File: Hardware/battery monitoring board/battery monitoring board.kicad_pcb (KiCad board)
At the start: 2 copper layers, 190.5 x 53.3 mm, 69 parts, among them J1 Conn_01x02, J2 Conn_01x02, J3 S5B-XH-A, J4 Conn_01x02, J5 Conn_01x02, J6 Conn_01x02, J7 Conn_01x02, J8 Conn_01x02, J9 S5B-XH-A, K1 Relay_SPST-NO, Q1 PNP, Q2 PN2222A, U1 MAX31855KASA

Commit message: Added more parts
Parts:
- moved J5 90.3 mm to (87.6, 43.2), turned to -90 degrees
- moved J4 87.3 mm to (88.9, 30.5), turned to -90 degrees
- moved J6 79.9 mm to (87.6, 50.8), turned to -90 degrees
- moved J7 69.6 mm to (87.6, 58.4), turned to -90 degrees
- moved J8 59.4 mm to (87.6, 66.0), turned to -90 degrees
- moved TP14 53.0 mm to (123.4, 27.2), turned to 90 degrees
- moved R23 46.8 mm to (114.8, 35.6), turned to 90 degrees
- moved R19 46.7 mm to (114.8, 23.9), turned to -90 degrees
- moved R21 46.6 mm to (114.8, 30.5), turned to -90 degrees
- moved R17 45.9 mm to (112.8, 39.9)
- moved TP15 45.1 mm to (119.9, 27.2), turned to 90 degrees
- moved R22 42.8 mm to (111.3, 35.6), turned to 90 degrees
- moved R18 42.8 mm to (111.3, 23.9), turned to 90 degrees
- moved R20 42.7 mm to (111.3, 30.5), turned to -90 degrees
- moved TP16 34.7 mm to (118.4, 43.9)
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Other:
- board size 190.5 x 53.3 mm -> 134.6 x 53.3 mm

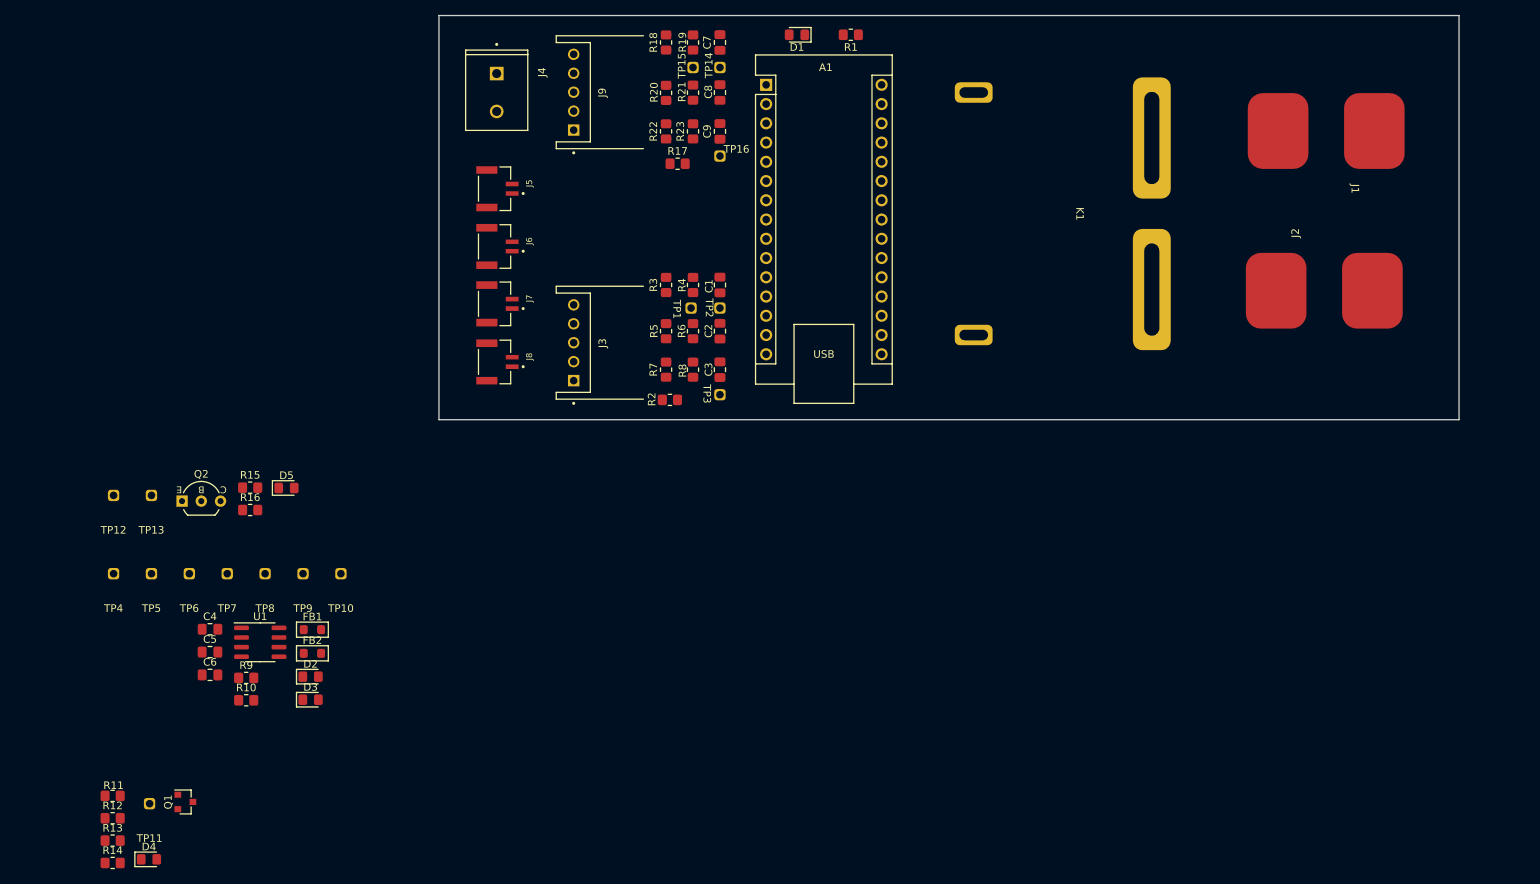
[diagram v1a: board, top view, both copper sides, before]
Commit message: place leak sensor and temp sensor on the pcb
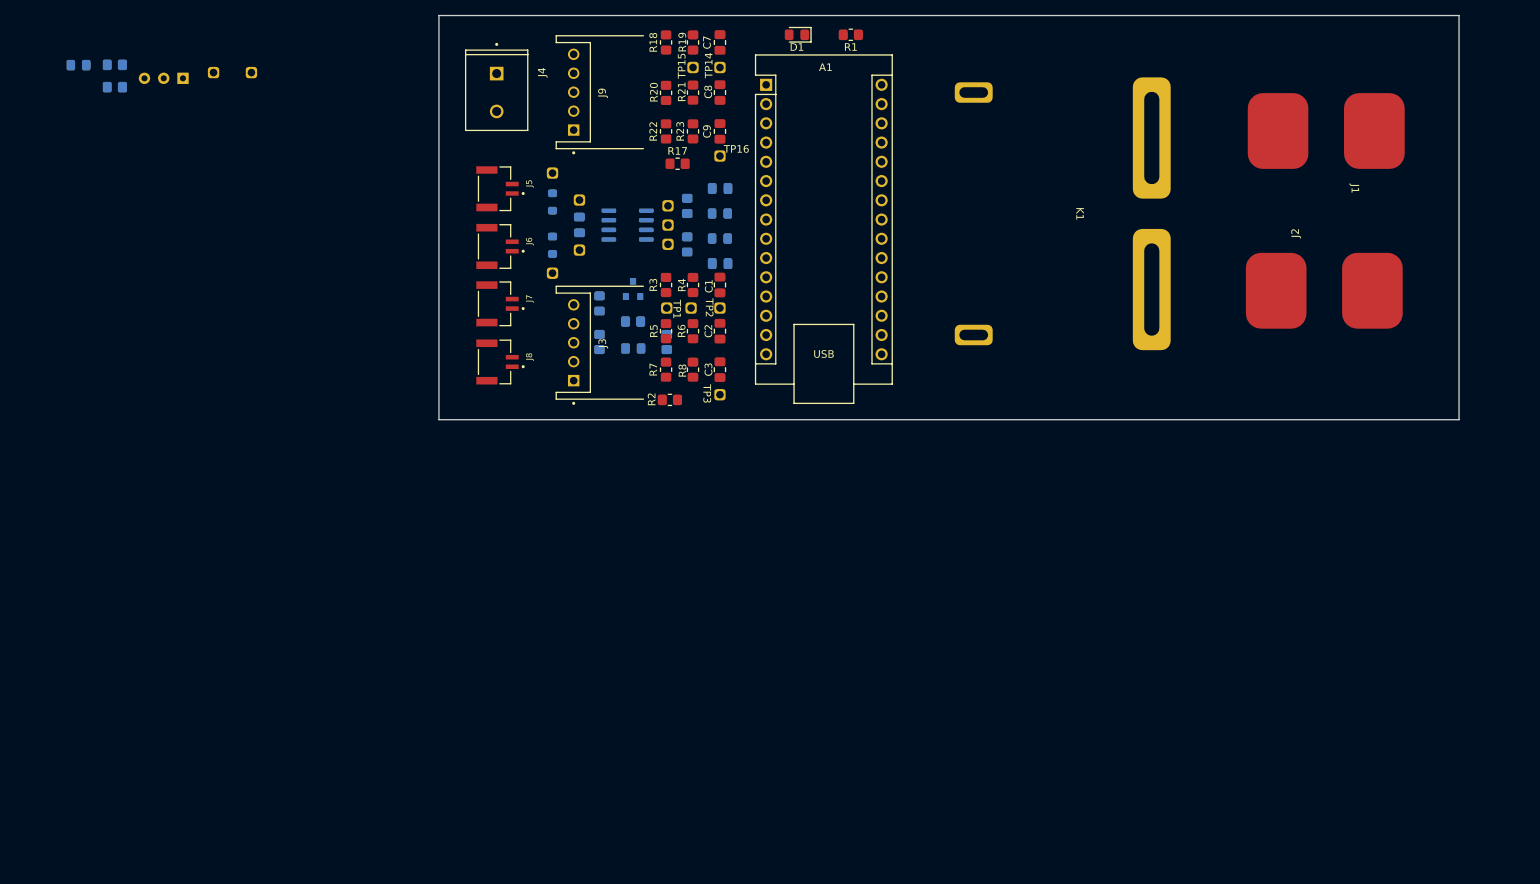
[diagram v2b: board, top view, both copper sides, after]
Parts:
- C4, C5, C6, D2, D3, D4, D5, FB1, FB2, Q1, Q2, R10, R11, R12, R13, R14, R15, R16, R9, TP10, TP11, TP12, TP13, TP4, TP5, TP6, TP7, TP8, TP9, U1: moved to B.Cu
- moved R14 100.4 mm to (111.3, 63.4), turned to -90 degrees
- moved R13 97.0 mm to (106.9, 60.7), turned to 180 degrees
- moved TP11 94.5 mm to (111.3, 64.0), turned to 180 degrees
- moved R12 93.5 mm to (102.5, 58.3), turned to -90 degrees
- moved D4 92.9 mm to (106.9, 64.3)
- moved C5 91.0 mm to (118.4, 43.1), turned to 180 degrees
- moved Q1 89.9 mm to (106.9, 56.4), turned to 90 degrees
- moved R11 87.8 mm to (102.5, 63.4), turned to 90 degrees
- moved C6 86.5 mm to (118.4, 53.1), turned to 180 degrees
- moved R9 85.2 mm to (114.0, 45.5), turned to -90 degrees
- moved R10 83.7 mm to (114.0, 50.5), turned to -90 degrees
- moved D2 81.6 mm to (118.4, 46.5), turned to 180 degrees
- moved D3 81.4 mm to (118.4, 49.8), turned to 180 degrees
- moved TP4 78.4 mm to (96.3, 46.2), turned to 180 degrees
- moved U1 73.4 mm to (106.2, 48.0)
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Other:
- copper layers 2 -> 4

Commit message: Added screw holes + other stuff
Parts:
- added ?: , , F.Cu at (83.8, 71.1)
- added ?: , , F.Cu at (213.6, 71.4)
- added ?: , , F.Cu at (213.4, 22.9)
- added J10: Conn_01x02, Library:JST_BM02B-GHS-TBT_LF__SN_, F.Cu at (88.4, 24.6)
- added REF**: Screw_Holes, Library:Screw_Holes, F.Cu at (83.8, 25.4)
- moved D5 128.3 mm to (160.5, 46.5), turned to -90 degrees
- moved TP13 116.6 mm to (159.5, 77.0)
- moved R16 112.6 mm to (149.4, 49.5), turned to -90 degrees
- moved R15 111.3 mm to (148.3, 45.0), turned to 0 degrees
- moved Q2 108.4 mm to (155.0, 42.3), turned to -90 degrees
- moved TP12 100.1 mm to (146.6, 76.7)
- moved J4 4.58 mm to (88.6, 35.1)
- moved J5 2.18 mm to (88.4, 45.2)
- moved J6 2.18 mm to (88.4, 52.8)
- moved J7 2.18 mm to (88.4, 60.4)
- moved J8 2.18 mm to (88.4, 68.1)
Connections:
- net +9V renamed Net-(D5-K)
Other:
- outline, holes or cut-outs redrawn

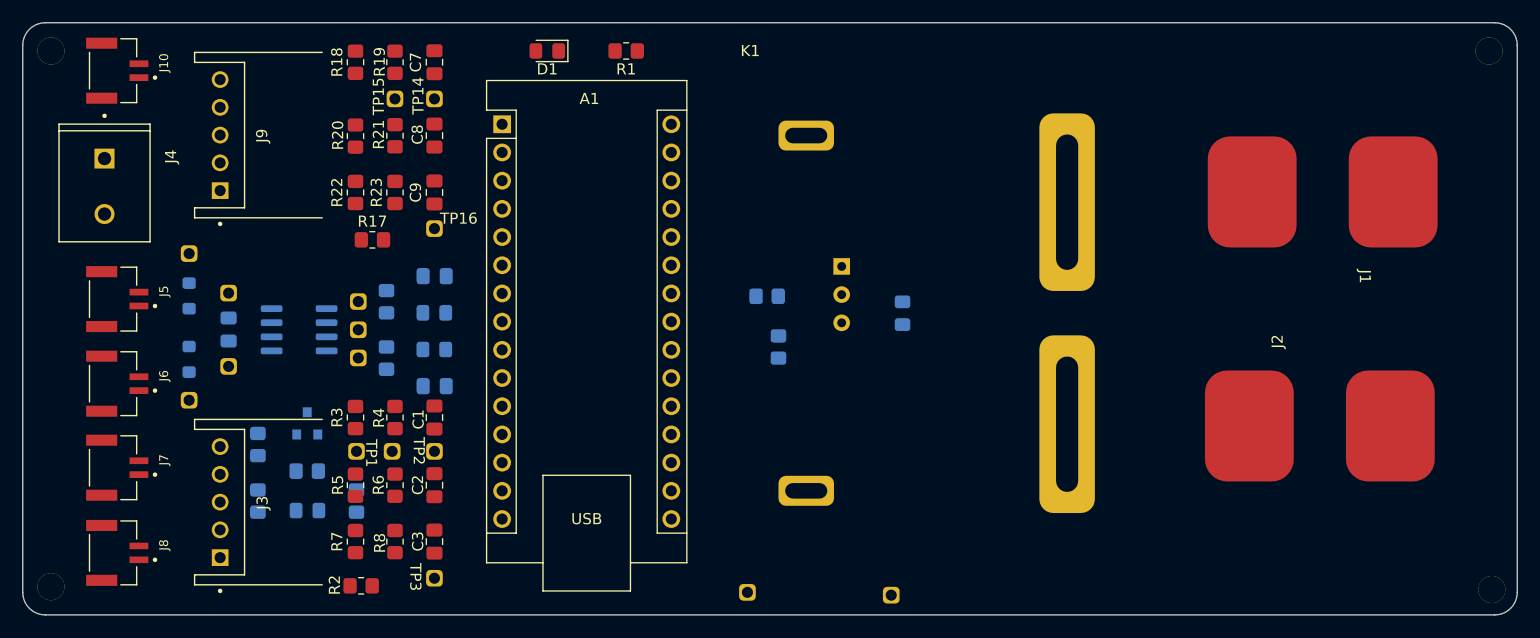
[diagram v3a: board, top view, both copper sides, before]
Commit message: Added traces pt.I
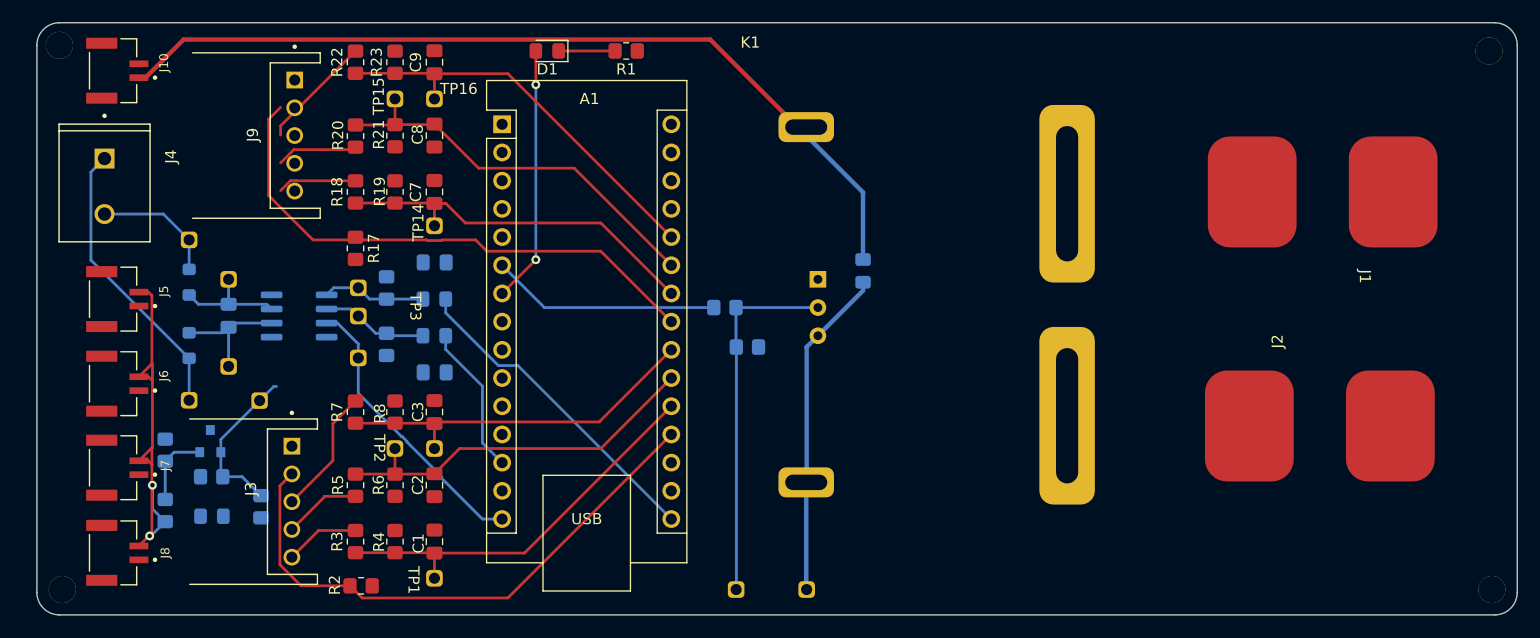
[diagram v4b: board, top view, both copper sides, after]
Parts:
- moved TP1 12.0 mm to (113.3, 70.4)
- moved C9 11.7 mm to (118.4, 23.9)
- moved R22 11.7 mm to (111.3, 23.9)
- moved R23 11.7 mm to (114.8, 23.9)
- moved TP3 11.7 mm to (113.3, 58.7)
- moved C7 11.7 mm to (118.4, 35.6)
- moved R18 11.7 mm to (111.3, 35.6)
- moved R19 11.7 mm to (114.8, 35.6)
- moved TP16 11.7 mm to (118.4, 32.3)
- moved C3 11.7 mm to (118.4, 55.4)
- moved R7 11.7 mm to (111.3, 55.4)
- moved R8 11.7 mm to (114.8, 55.4)
- moved TP14 11.4 mm to (123.4, 38.6)
- moved C1 11.2 mm to (118.4, 67.1)
- moved R3 11.2 mm to (111.3, 67.1)
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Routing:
- net Net-(D5-K): track 0.00 -> 78.4 mm
- net /voltage monitor/OUT1: track 0.00 -> 51.2 mm
- net /voltage monitor2/OUT1: track 0.00 -> 49.4 mm
- net /voltage monitor2/OUT4: track 0.00 -> 36.8 mm
- net /voltage monitor/OUT2: track 0.00 -> 36.2 mm
- net /leak sensor/PROBE: track 0.00 -> 36.1 mm, vias 0 -> 2
- net /voltage monitor2/OUT3: track 0.00 -> 36.1 mm
- net /voltage monitor/OUT3: track 0.00 -> 34.3 mm
- net /voltage monitor2/OUT2: track 0.00 -> 34.1 mm
- net /voltage monitor/OUT4: track 0.00 -> 33.5 mm
- net Net-(Q2-B): track 0.00 -> 33.2 mm
- net Net-(D5-A): track 0.00 -> 30.1 mm
- net /temp sensor/sck: track 0.00 -> 29.3 mm
- net /temp sensor/so: track 0.00 -> 26.0 mm
- net Net-(J4-Pin_1): track 0.00 -> 25.9 mm
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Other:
- board size 134.6 x 53.3 mm -> 133.4 x 53.3 mm

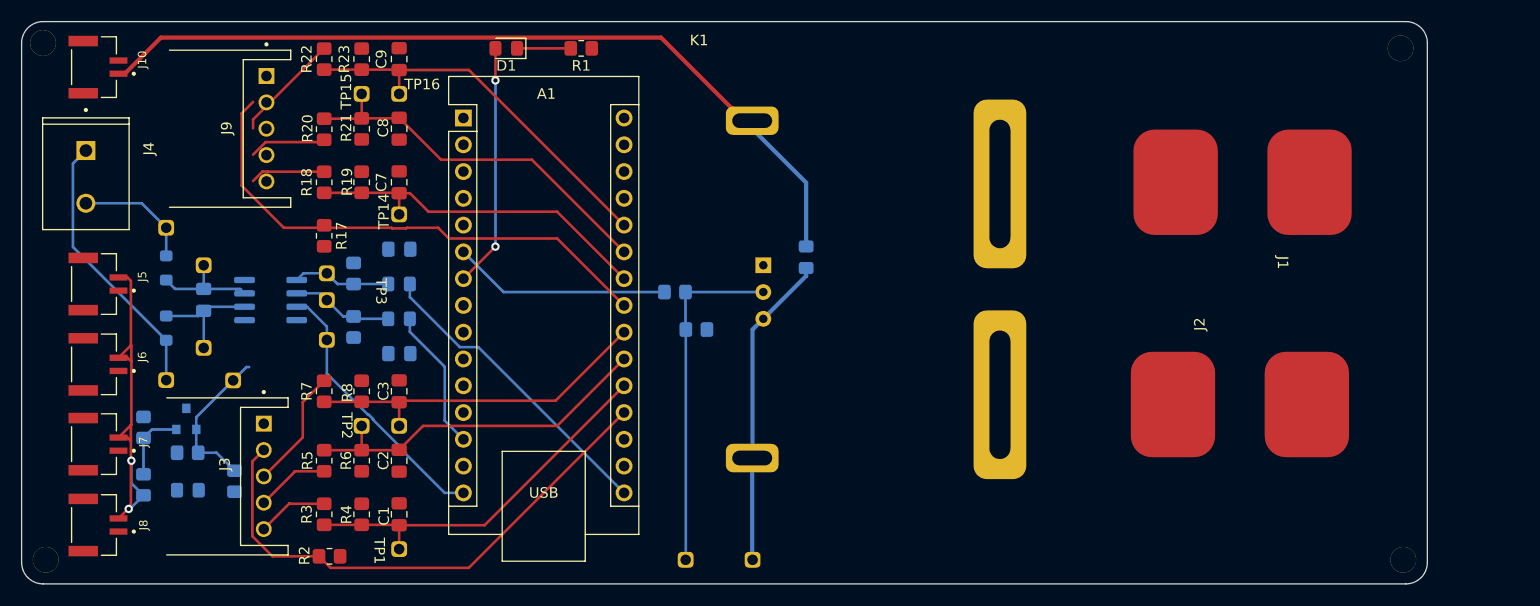
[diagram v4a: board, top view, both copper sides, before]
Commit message: Added traces pt.II
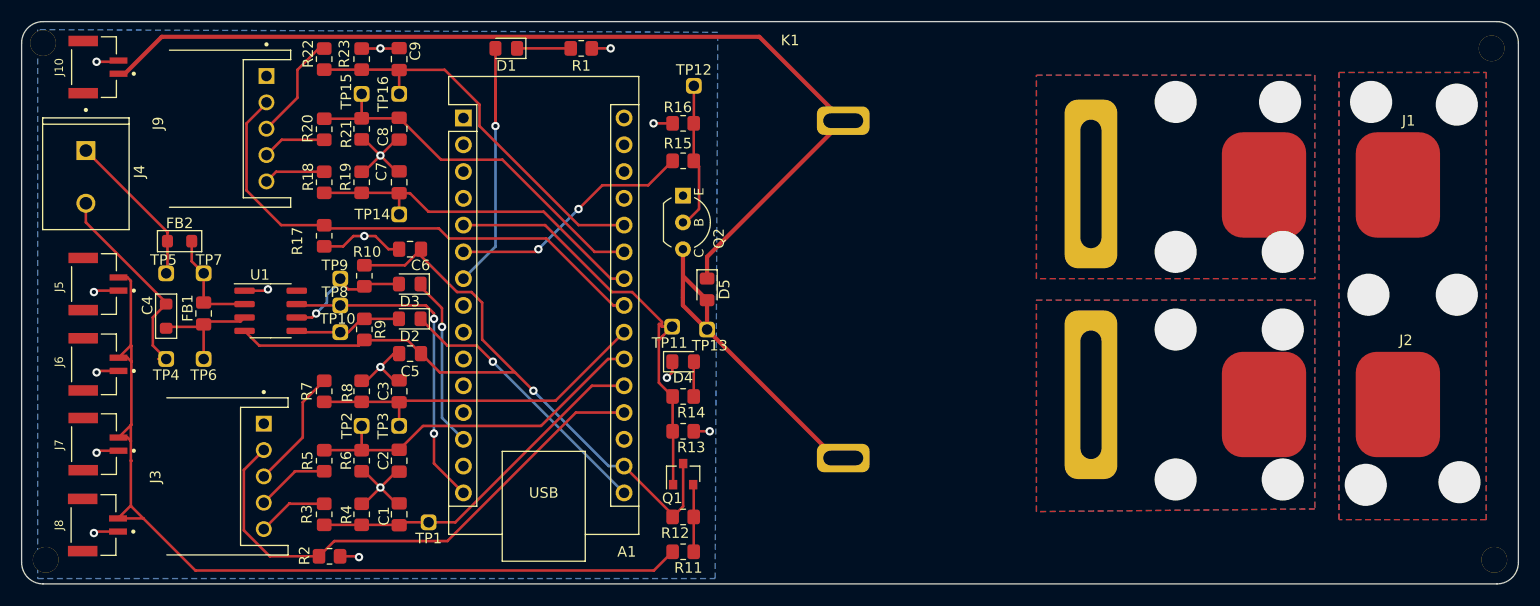
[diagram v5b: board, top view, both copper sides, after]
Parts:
- C4, C5, C6, D2, D3, D4, D5, FB1, FB2, Q1, Q2, R10, R11, R12, R13, R14, R15, R16, R9, TP10, TP4, TP6, TP9, U1: moved to F.Cu
- moved R12 51.9 mm to (145.3, 67.3), turned to 0 degrees
- moved R11 51.6 mm to (145.3, 70.6), turned to 0 degrees
- moved D4 48.5 mm to (145.3, 52.6)
- moved Q1 47.4 mm to (145.3, 63.2)
- moved R13 47.0 mm to (145.3, 59.2), turned to 0 degrees
- moved TP12 45.0 mm to (146.3, 31.5)
- moved R14 43.3 mm to (145.3, 55.9), turned to 0 degrees
- moved TP11 42.0 mm to (144.3, 54.3)
- moved TP13 22.3 mm to (147.6, 54.6)
- moved R16 19.6 mm to (145.3, 30.0), turned to 180 degrees
- moved R15 12.5 mm to (145.3, 33.5)
- moved TP9 12.3 mm to (112.8, 39.6)
- moved TP5 10.1 mm to (96.3, 49.3)
- moved Q2 10.1 mm to (145.3, 36.8)
- moved C5 9.96 mm to (119.4, 51.8)
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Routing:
- net +3V3: track 0.00 -> 76.2 mm, vias 0 -> 1
- net GND: track 0.00 -> 59.9 mm, vias 0 -> 22
- net /leak sensor/PROBE: track 36.1 -> 87.5 mm, vias 2 -> 0
- net /leak sensor/LEAK_SIGNAL: track 14.6 -> 41.8 mm
- net Net-(Q2-B): track 33.2 -> 14.1 mm
- net Net-(D5-K): track 78.4 -> 93.8 mm
- net Net-(J4-Pin_1): track 25.9 -> 14.9 mm
- net Net-(J4-Pin_2): track 11.2 -> 19.5 mm
- net /temp sensor/so: track 26.0 -> 31.6 mm, vias 0 -> 2
- net Net-(A1-D4): track 23.1 -> 27.4 mm, vias 2 -> 1
- net /e-switch/MCU_OUTPUT: track 20.4 -> 23.8 mm, vias 0 -> 2
- net Net-(D4-A): track 0.00 -> 3.41 mm
- net /temp sensor/sck: track 29.3 -> 26.1 mm, vias 0 -> 1
- net /temp sensor/cs: track 13.5 -> 16.4 mm, vias 0 -> 1
- net Net-(D3-A): track 9.68 -> 12.3 mm, vias 0 -> 1
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- added copper zone on B.Cu, net /e-switch/BATTERY_IN
- added copper zone on F.Cu, net /e-switch/BATTERY_IN
- added copper zone on B.Cu, net /e-switch/SYSTEM_POWER
- added copper zone on F.Cu, net /e-switch/SYSTEM_POWER
- added copper zone on B.Cu, net GND
- added copper zone on F.Cu, net GND
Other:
- board size 133.4 x 53.3 mm -> 142 x 53.3 mm

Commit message: more pcb work
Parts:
- removed ? (x3): , 
- removed REF**: Screw_Holes, Library:Screw_Holes
- added G***: LOGO, LOGO, F.Cu at (200.4, 70.1)
- J10 9V: renamed from J10
- moved J8 1.18 mm to (89.5, 68.1)
- moved J10 9V 1.02 mm to (89.4, 24.6)
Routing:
- net GND: track 59.9 -> 62.6 mm
- net /leak sensor/PROBE: track 87.5 -> 85.8 mm
- net Net-(D5-K): track 93.8 -> 93.2 mm
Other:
- outline, holes or cut-outs redrawn

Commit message: cleaned up traces
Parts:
- moved TP13 0.25 mm to (147.6, 54.4)
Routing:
- net Net-(D5-A): track 32.4 -> 26.7 mm
- net /leak sensor/PROBE: track 85.8 -> 81.5 mm
- net /leak sensor/LEAK_SIGNAL: track 41.8 -> 39.7 mm

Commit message: updated pcb
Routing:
- net GND: vias 22 -> 117
- net /e-switch/SYSTEM_POWER: vias 4 -> 73
- net /e-switch/BATTERY_IN: vias 4 -> 73
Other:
- outline, holes or cut-outs redrawn
